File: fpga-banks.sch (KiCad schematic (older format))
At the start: 56 parts, among them J13 62000311121, Q12 2N7002, Q13 2N7002, Q14 2N7002, Q15 2N7002, Q16 2N7002, U14 XC7A100T-FGG484

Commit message: Updated voltage supply labels, connected gpios left
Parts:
- added R?: R_0R_0402, artix-dc-scm-footprints:0402-res, symbol artix-dc-scm:R_0R_0402
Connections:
- net labels added: PRSNT0_N_R, VCC1V35, VIRTUAL_RESEAT_R
- net labels removed: DDR3_CS, VCC1V35_BANK, VCC1V8_BANK, VCC3V3_BANK
- wire segments 395 -> 397
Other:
- moved on the sheet: C178, D10, D11, D12, D13, D9, J13, PROG_B1, Q12, Q13, Q14, Q15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

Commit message: Typo fix
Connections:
- net labels added: SPI0_CLK, SPI0_CLK_R, SPI0_CS_N, SPI0_CS_N_R, SPI0_MISO, SPI0_MISO_R, SPI0_MOSI, SPI0_MOSI_R
- net labels removed: SPIO_CLK, SPIO_CLK_R, SPIO_CS_N, SPIO_CS_N_R, SPIO_MISO, SPIO_MISO_R, SPIO_MOSI, SPIO_MOSI_R
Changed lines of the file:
@@
 	3850 7600 3950 7600
 Text GLabel 2175 8200 2    50   Input ~ 0
-SPIO_CLK
+SPI0_CLK
 Text GLabel 2175 8000 2    50   Input ~ 0
-SPIO_CS_N
+SPI0_CS_N
 Text GLabel 2175 7600 2    50   Input ~ 0
-SPIO_MOSI
+SPI0_MOSI
 Text GLabel 2175 7800 2    50   Input ~ 0
-SPIO_MISO
+SPI0_MISO
 Wire Wire Line
 	11600 3200 12000 3200
@@
 	6325 6950 6700 6950
 Text GLabel 1425 8200 0    50   Input ~ 0
-SPIO_CLK_R
+SPI0_CLK_R
 Text GLabel 1425 8000 0    50   Input ~ 0
-SPIO_CS_N_R
+SPI0_CS_N_R
 Text GLabel 1425 7600 0    50   Input ~ 0
-SPIO_MOSI_R
+SPI0_MOSI_R
 Text GLabel 1425 7800 0    50   Input ~ 0
-SPIO_MISO_R
+SPI0_MISO_R
 Wire Wire Line
 	1425 7600 1800 7600
@@
 	1425 8200 1800 8200
 Text GLabel 9725 2950 2    50   Input ~ 0
-SPIO_CLK_R
+SPI0_CLK_R
 Text GLabel 9725 3050 2    50   Input ~ 0
-SPIO_CS_N_R
+SPI0_CS_N_R
 Text GLabel 9725 3850 2    50   Input ~ 0
-SPIO_MOSI_R
+SPI0_MOSI_R
 Text GLabel 9725 3450 2    50   Input ~ 0
-SPIO_MISO_R
+SPI0_MISO_R
 Wire Wire Line
 	9500 3450 9725 3450

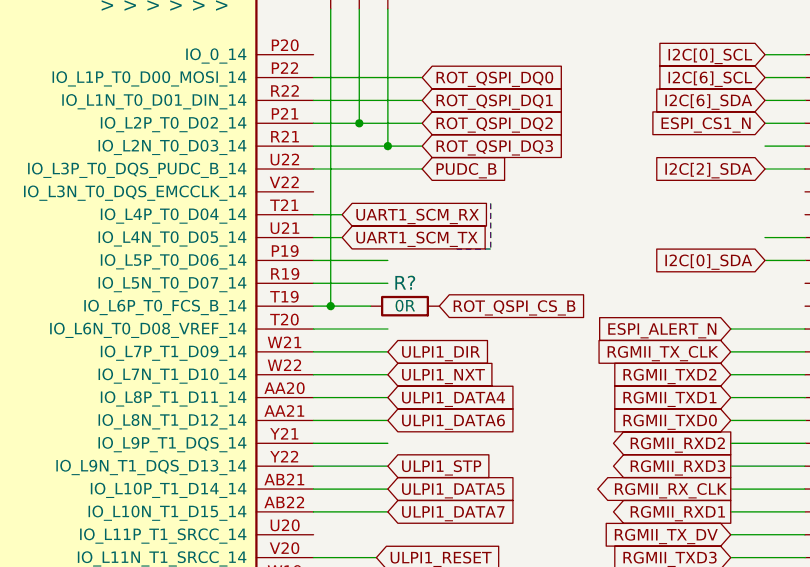
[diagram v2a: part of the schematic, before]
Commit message: Replaced RoT connector with higher one
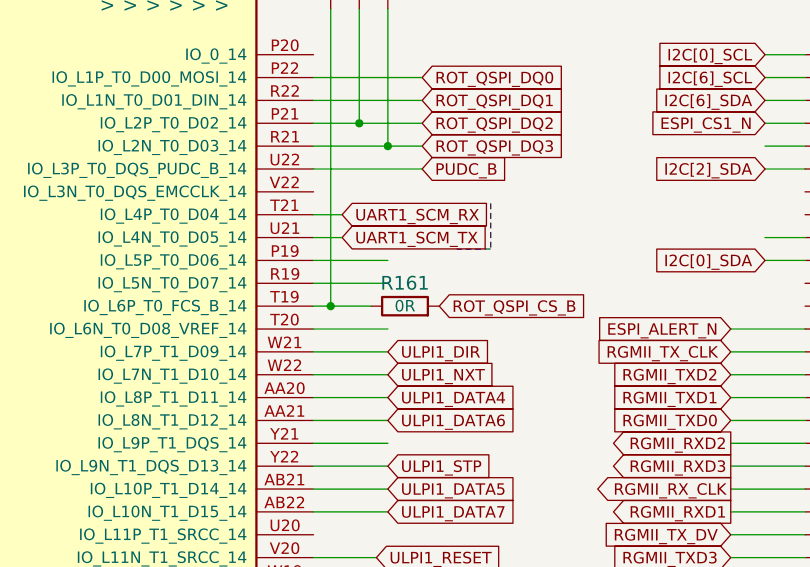
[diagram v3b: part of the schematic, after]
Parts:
- gave numbers to parts that had none: 1
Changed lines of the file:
@@
 VCC3V3
 $Comp
-L artix-dc-scm:R_0R_0402 R?
+L artix-dc-scm:R_0R_0402 R161
 U 1 1 60D5BDB3
 P 4950 3150
-F 0 "R?" H 4950 3250 60  0000 C CNN
+F 0 "R161" H 4950 3250 60  0000 C CNN
 F 1 "R_0R_0402" H 4950 3000 60  0001 C CNN
 F 2 "artix-dc-scm-footprints:0402-res" H 5150 3350 60  0001 L CNN

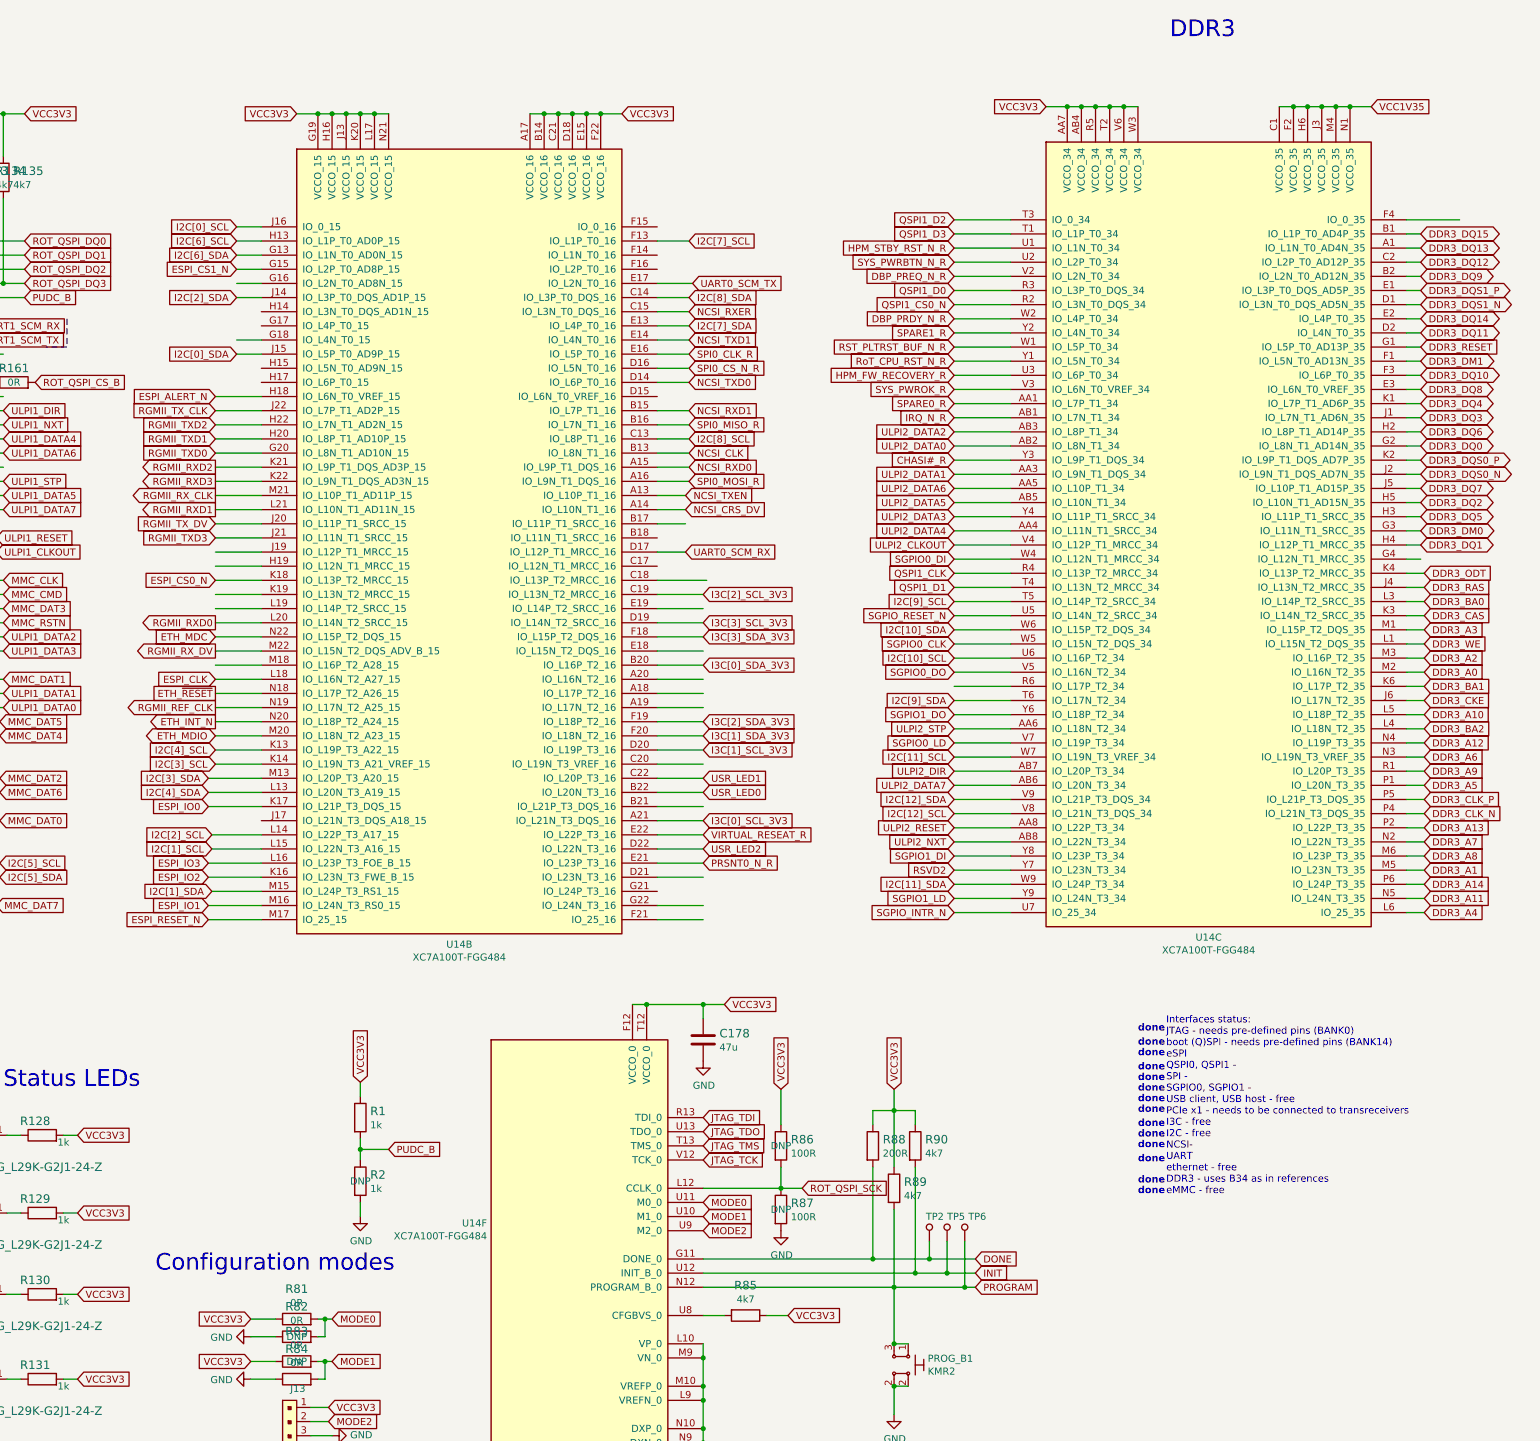
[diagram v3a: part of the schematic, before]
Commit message: Add FPGA 100MHz clock source
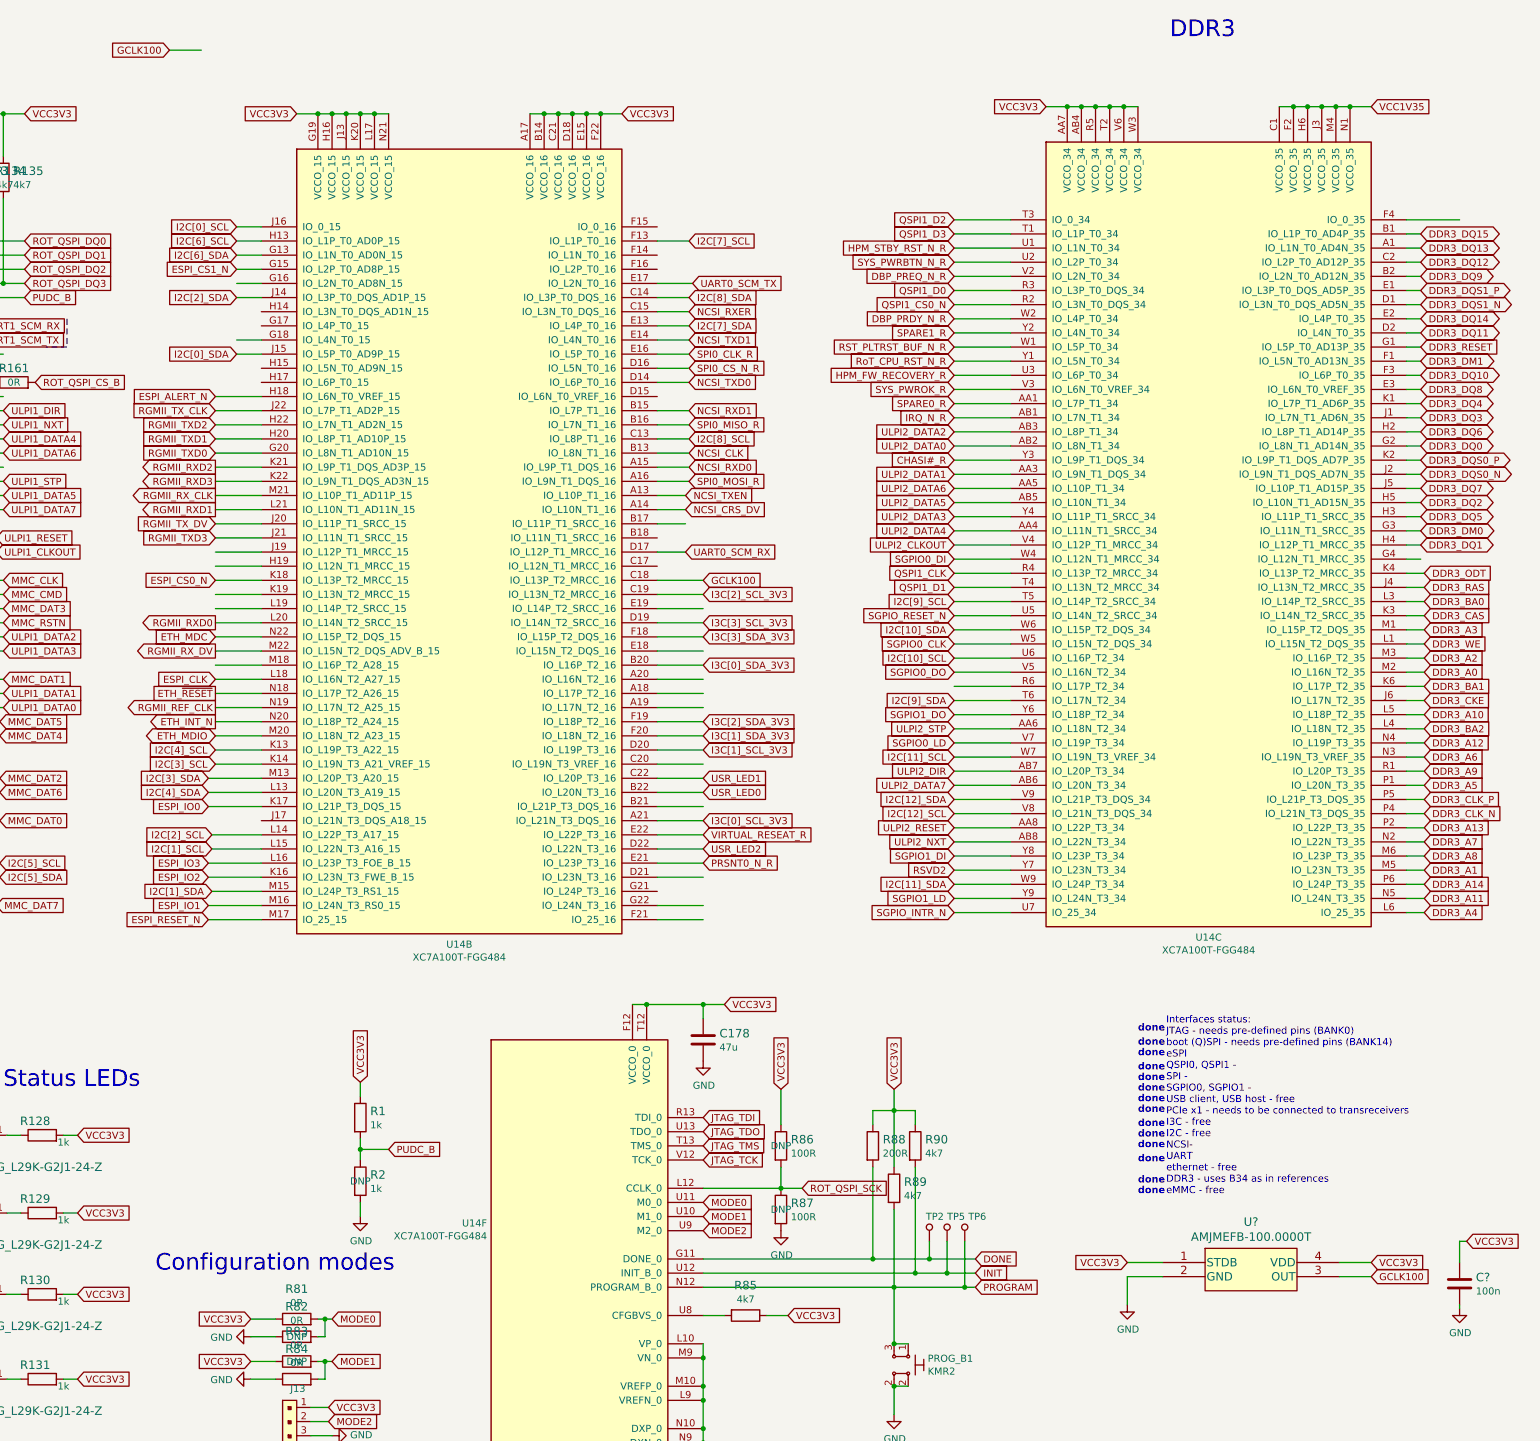
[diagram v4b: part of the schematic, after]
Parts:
- added C?: C_100n_0402, antmicro-footprints:0402-cap, symbol antmicroCapacitors0402:C_100n_0402
- added U?: AMJMEFB-100.0000T, antmicro-footprints:AMJMEFB, symbol antmicroOscillators:AMJMEFB-100.0000T
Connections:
- net labels added: GCLK100
- wire segments 397 -> 406
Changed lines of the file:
@@
 	9500 5550 9825 5550
 Wire Wire Line
-	9850 4550 9500 4550
+	9825 4550 9500 4550
 Wire Wire Line
 	9500 4350 9700 4350
@@
 Text GLabel 9825 6550 2    50   Input ~ 0
 PRSNT0_N_R
+$Comp
+L antmicroOscillators:AMJMEFB-100.0000T U?
+U 1 1 6063C254
+P 13075 9375
+F 0 "U?" H 13700 9662 60  0000 C CNN
+F 1 "AMJMEFB-100.0000T" H 13700 9556 60  0000 C CNN
+F 2 "antmicro-footprints:AMJMEFB" H 13875 9615 60  0001 C CNN
+F 3 "" H 13075 9375 60  0000 C CNN
+F 4 "AMJMEFB-100.0000T" H 13075 9375 50  0001 C CNN "MPN"
+F 5 "Abracon" H 13075 9375 50  0001 C CNN "Field5"
+	1    13075 9375
+	1    0    0    -1
+$EndComp
+Wire Wire Line
+	14325 9475 14550 9475
+Wire Wire Line
+	13075 9475 12825 9475
+Wire Wire Line
+	12825 9475 12825 9675
+$Comp
+L artix-dc-scm:GND-artix-dc-scm #PWR?
+U 1 1 60702573
+P 12825 9675
+F 0 "#PWR?" H 12825 9425 50  0001 C CNN
+F 1 "GND" H 12830 9502 50  0000 C CNN
+F 2 "" H 12825 9675 50  0001 C CNN
+F 3 "" H 12825 9675 50  0001 C CNN
+	1    12825 9675
+	1    0    0    -1
+$EndComp
+$Comp
+L antmicroCapacitors0402:C_100n_0402 C?
+U 1 1 60752952
+P 15175 9525
+F 0 "C?" H 15290 9570 60  0000 L CNN
+F 1 "C_100n_0402" H 15175 9375 60  0001 C CNN
+F 2 "antmicro-footprints:0402-cap" H 15375 9725 60  0001 L CNN
+F 3 "" H 15175 9525 50  0001 C CNN
+F 4 "Walsin" H 15375 9925 60  0001 L CNN "Manufacturer"
+F 5 "0402X104K6R3CT" H 15375 9825 60  0001 L CNN "MPN"
+F 6 "100n" H 15290 9472 50  0000 L CNN "Val"
+	1    15175 9525
+	1    0    0    -1
+$EndComp
+$Comp
+L artix-dc-scm:GND-artix-dc-scm #PWR?
+U 1 1 6094150C
+P 15175 9700
+F 0 "#PWR?" H 15175 9450 50  0001 C CNN
+F 1 "GND" H 15180 9527 50  0000 C CNN
+F 2 "" H 15175 9700 50  0001 C CNN
+F 3 "" H 15175 9700 50  0001 C CNN
+	1    15175 9700
+	1    0    0    -1
+$EndComp
+Wire Wire Line
+	15175 9700 15175 9675
+Text GLabel 12825 9375 0    50   Input ~ 0
+VCC3V3
+Wire Wire Line
+	12825 9375 13075 9375
+Text GLabel 14550 9375 2    50   Input ~ 0
+VCC3V3
+Wire Wire Line
+	14325 9375 14550 9375
+Text GLabel 14550 9475 2    50   Input ~ 0
+GCLK100
+Text GLabel 15225 9225 2    50   Input ~ 0
+VCC3V3
+Wire Wire Line
+	15175 9375 15175 9225
+Wire Wire Line
+	15175 9225 15225 9225
+Wire Wire Line
+	6275 800  6050 800
+Text GLabel 6050 800  0    50   Input ~ 0
+GCLK100
+Text GLabel 9825 4550 2    50   Input ~ 0
+GCLK100
 $EndSCHEMATC

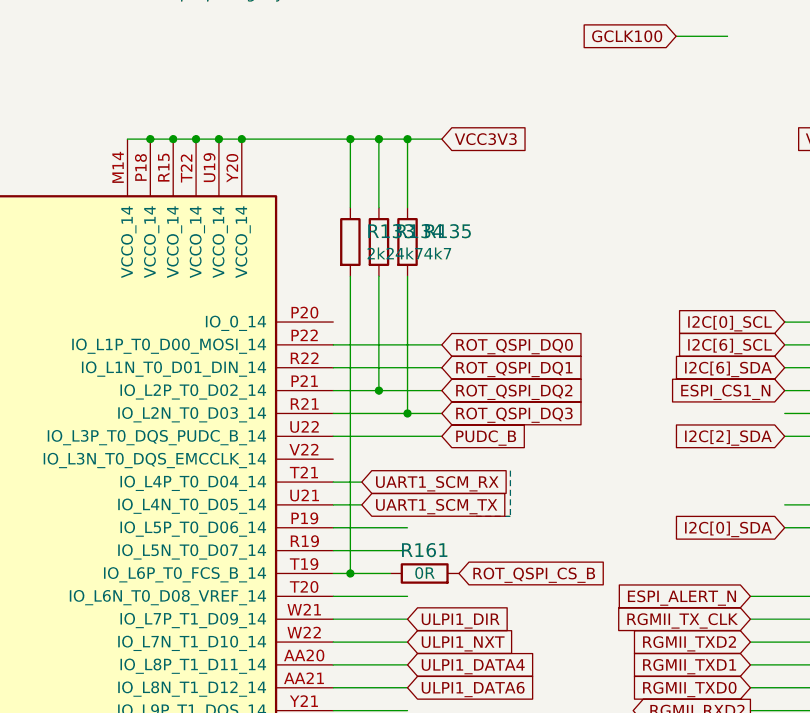
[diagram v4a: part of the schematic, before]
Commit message: Route configuration QSPI
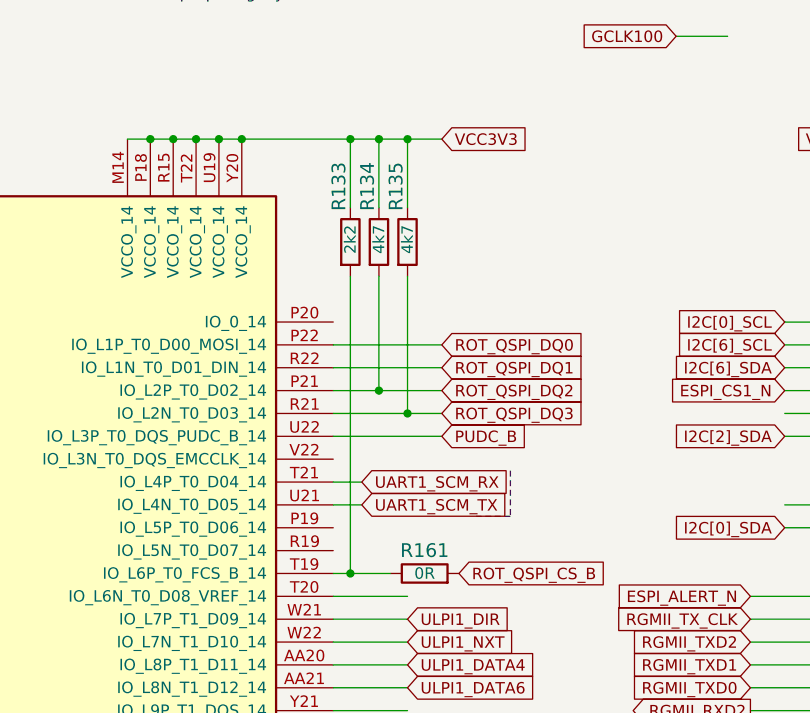
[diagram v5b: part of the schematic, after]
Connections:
- wire segments 406 -> 404
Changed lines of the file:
@@
 	4675 2850 4550 2850
-Wire Wire Line
-	4875 2950 4550 2950
-Wire Wire Line
-	4875 3050 4550 3050
 Wire Wire Line
 	4800 3150 4625 3150
@@
 U 1 1 601DDEB8
 P 4625 1700
-F 0 "R133" V 4580 1770 60  0000 L CNN
+F 0 "R133" H 4275 1650 60  0000 L CNN
 F 1 "R_2k2_0402" H 4625 1550 60  0001 C CNN
 F 2 "artix-dc-scm-footprints:0402-res" H 4825 1900 60  0001 L CNN
@@
 F 4 "YAGEO" H 4825 2100 60  0001 L CNN "Manufacturer"
 F 5 "RC0402FR-072K2L" H 4825 2000 60  0001 L CNN "MPN"
-F 6 "2k2" V 4678 1770 50  0000 L CNN "Val"
+F 6 "2k2" H 4550 1700 50  0000 L CNN "Val"
 	1    4625 1700
 	0    1    1    0
@@
 U 1 1 601DFDEE
 P 4750 1700
-F 0 "R134" V 4705 1770 60  0000 L CNN
+F 0 "R134" H 4400 1650 60  0000 L CNN
 F 1 "R_4k7_0402" H 4750 1550 60  0001 C CNN
 F 2 "artix-dc-scm-footprints:0402-res" H 4950 1900 60  0001 L CNN
@@
 F 4 "PANASONIC_ELECTRONIC_COMPONENTS" H 4950 2100 60  0001 L CNN "Manufacturer"
 F 5 "ERJ2GEJ472X" H 4950 2000 60  0001 L CNN "MPN"
-F 6 "4k7" V 4803 1770 50  0000 L CNN "Val"
+F 6 "4k7" H 4675 1700 50  0000 L CNN "Val"
 	1    4750 1700
 	0    1    1    0
@@
 U 1 1 601E0616
 P 4875 1700
-F 0 "R135" V 4830 1770 60  0000 L CNN
+F 0 "R135" H 4525 1650 60  0000 L CNN
 F 1 "R_4k7_0402" H 4875 1550 60  0001 C CNN
 F 2 "artix-dc-scm-footprints:0402-res" H 5075 1900 60  0001 L CNN
@@
 F 4 "PANASONIC_ELECTRONIC_COMPONENTS" H 5075 2100 60  0001 L CNN "Manufacturer"
 F 5 "ERJ2GEJ472X" H 5075 2000 60  0001 L CNN "MPN"
-F 6 "4k7" V 4928 1770 50  0000 L CNN "Val"
+F 6 "4k7" H 4800 1700 50  0000 L CNN "Val"
 	1    4875 1700
 	0    1    1    0

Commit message: Update DDR3 termination
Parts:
- gave numbers to parts that had none: 2
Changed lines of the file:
@@
 PRSNT0_N_R
 $Comp
-L antmicroOscillators:AMJMEFB-100.0000T U?
+L antmicroOscillators:AMJMEFB-100.0000T U15
 U 1 1 6063C254
 P 13075 9375
-F 0 "U?" H 13700 9662 60  0000 C CNN
+F 0 "U15" H 13700 9662 60  0000 C CNN
 F 1 "AMJMEFB-100.0000T" H 13700 9556 60  0000 C CNN
 F 2 "antmicro-footprints:AMJMEFB" H 13875 9615 60  0001 C CNN
@@
 	12825 9475 12825 9675
 $Comp
-L artix-dc-scm:GND-artix-dc-scm #PWR?
+L artix-dc-scm:GND-artix-dc-scm #PWR0101
 U 1 1 60702573
 P 12825 9675
-F 0 "#PWR?" H 12825 9425 50  0001 C CNN
+F 0 "#PWR0101" H 12825 9425 50  0001 C CNN
 F 1 "GND" H 12830 9502 50  0000 C CNN
 F 2 "" H 12825 9675 50  0001 C CNN
@@
 $EndComp
 $Comp
-L antmicroCapacitors0402:C_100n_0402 C?
+L antmicroCapacitors0402:C_100n_0402 C233
 U 1 1 60752952
 P 15175 9525
-F 0 "C?" H 15290 9570 60  0000 L CNN
+F 0 "C233" H 15290 9570 60  0000 L CNN
 F 1 "C_100n_0402" H 15175 9375 60  0001 C CNN
 F 2 "antmicro-footprints:0402-cap" H 15375 9725 60  0001 L CNN
@@
 $EndComp
 $Comp
-L artix-dc-scm:GND-artix-dc-scm #PWR?
+L artix-dc-scm:GND-artix-dc-scm #PWR0102
 U 1 1 6094150C
 P 15175 9700
-F 0 "#PWR?" H 15175 9450 50  0001 C CNN
+F 0 "#PWR0102" H 15175 9450 50  0001 C CNN
 F 1 "GND" H 15180 9527 50  0000 C CNN
 F 2 "" H 15175 9700 50  0001 C CNN
